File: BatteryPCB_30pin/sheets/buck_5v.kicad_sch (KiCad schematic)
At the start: 17 parts, among them U1 LMR51430XFDDCR

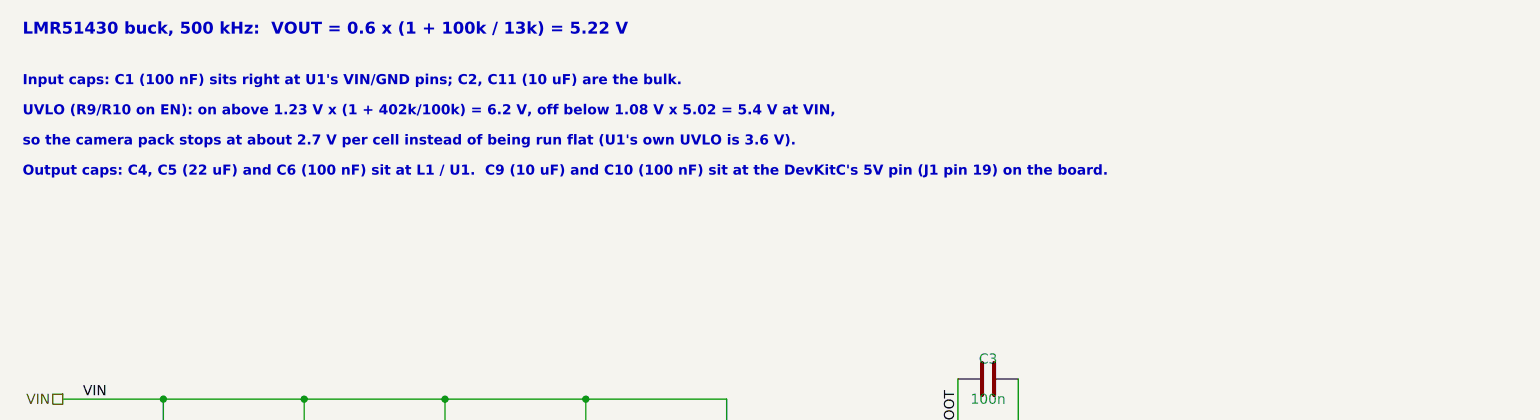
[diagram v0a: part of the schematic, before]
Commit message: Battery PCB 30-pin: XT30 and battery-holder holes to the datasheets; notes, check script
- XT30 J5/J6 pin holes 1.8 -> 1.9 mm (Amass drawing: 1.9 mm for the
  1.6 mm pins); 0.55 mm copper ring left on the 3.0 mm pads.
- Keystone 1042 holder peg holes 3.45 -> 3.5 mm and locator hole
  2.39 -> 2.4 mm on BT1-BT4 (Keystone M65p27; positions unchanged).
  Footprints updated in battery_pcb.pretty and on the board.
- Only those 16 hole sizes changed on the board: no part, trace, via,
  outline or silk moved. Tightest new gap: COTS_SW to a BT4 peg hole
  0.375 mm (rule 0.3).
- Schematic notes brought up to date: Q1 drop ~0.05 V (was 0.35 V from
  the old diode), J5/J6 are XT30 not Micro-Fit, C9/C10 sit at the
  ESP32's VIN (J1-15).
- verify_A: the old "seven edge cut-outs" count is replaced by a real
  check (7 rim notches + 4 square zip-tie cut-outs); ALL PASS, 36 checks.
- Gerbers, order-package zip, schematic PDF, project zip and STEP
  regenerated; BOM and CPL unchanged.

ERC 0 errors, DRC 0 (schematic parity, zones refilled, same 3
documented exclusions).

Co-Authored-By: Claude Opus 5.5 <noreply@anthropic.com>
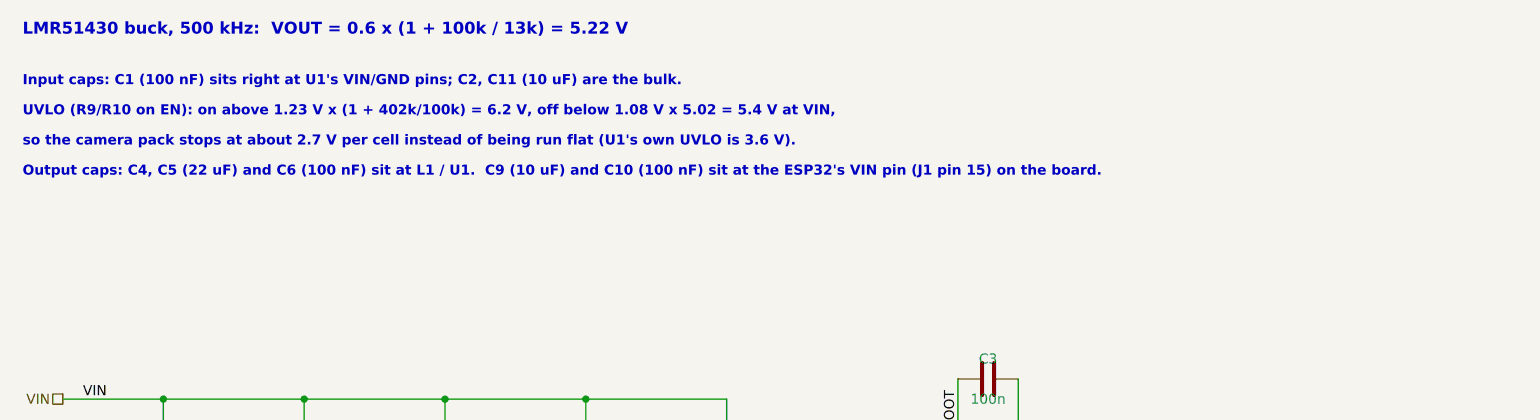
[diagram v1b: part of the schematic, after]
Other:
- note added: "Output caps: C4, C5 (22 uF) and C6 (100 nF) sit at L1 / U1. C9 (10 uF) and C10 (100 nF) sit at the ESP32's VIN pin (J1 pin 15) on the board."
- note removed: "Output caps: C4, C5 (22 uF) and C6 (100 nF) sit at L1 / U1. C9 (10 uF) and C10 (100 nF) sit at the DevKitC's 5V pin (J1 pin 19) on the board."
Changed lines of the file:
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@@
 		)
 	)
-	(text "Output caps: C4, C5 (22 uF) and C6 (100 nF) sit at L1 / U1.  C9 (10 uF) and C10 (100 nF) sit at the DevKitC's 5V pin (J1 pin 19) on the board."
+	(text "Output caps: C4, C5 (22 uF) and C6 (100 nF) sit at L1 / U1.  C9 (10 uF) and C10 (100 nF) sit at the ESP32's VIN pin (J1 pin 15) on the board."
 		(exclude_from_sim no)
 		(at 25.4 48.26 0)
